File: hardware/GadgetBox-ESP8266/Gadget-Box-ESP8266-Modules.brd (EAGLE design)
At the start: 93.5 x 53.5 mm, 23 parts

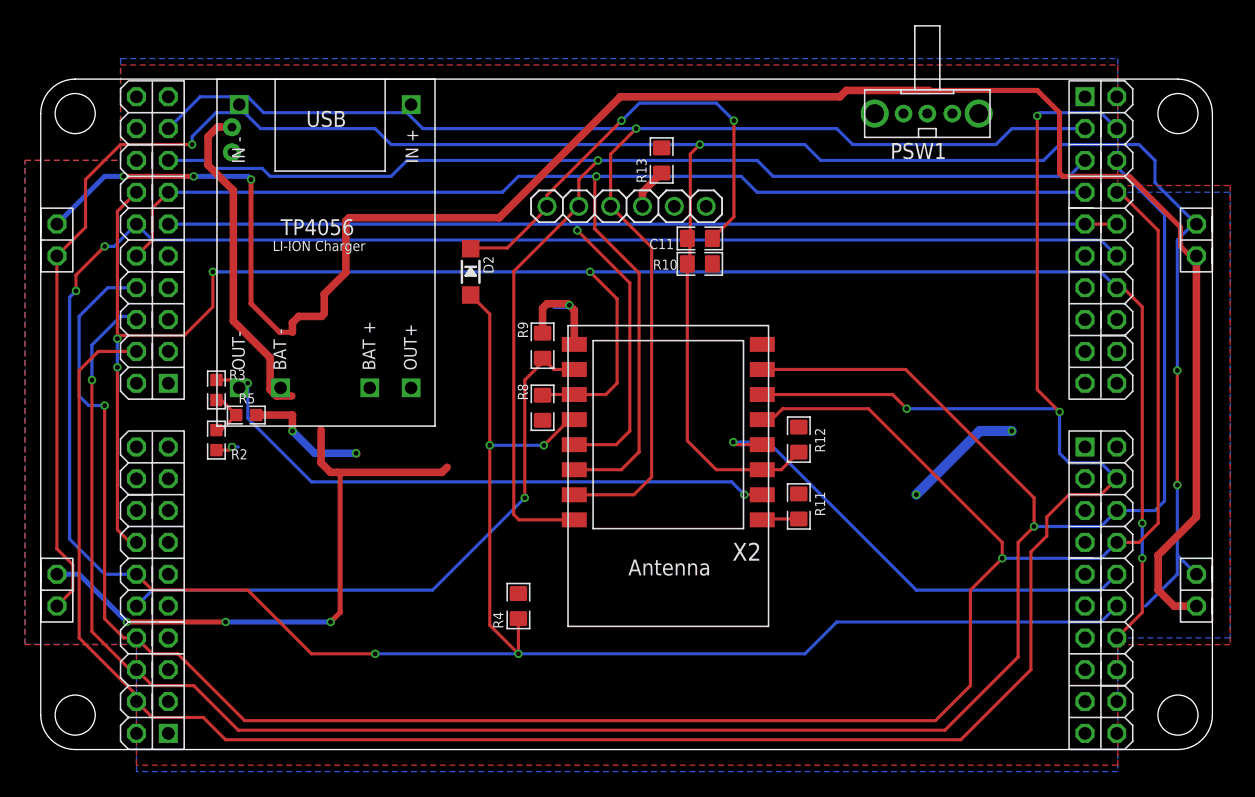
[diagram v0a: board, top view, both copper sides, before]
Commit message: Added battery cutouts and re-routed everything.
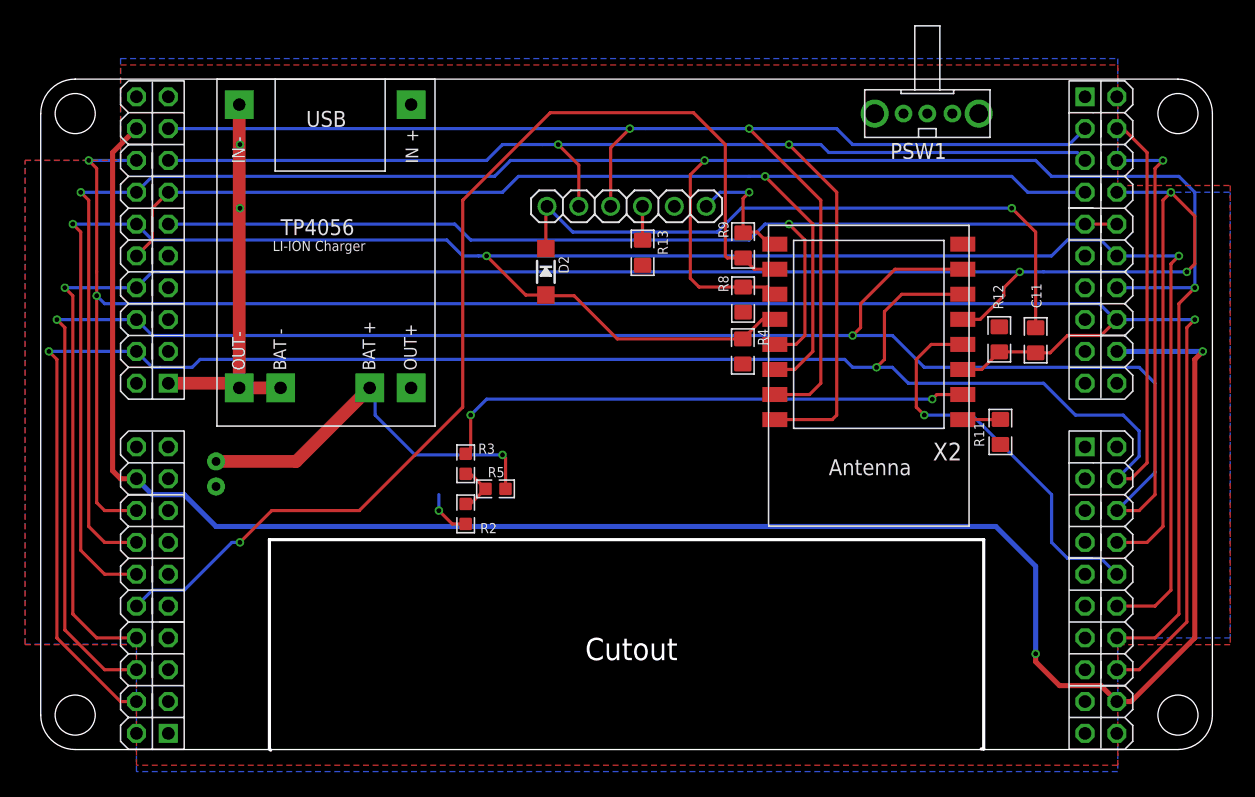
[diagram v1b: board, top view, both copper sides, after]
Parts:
- removed R10: 10K, GadgetFactory:0805
- AH, AL, BH, BL: value ECOGECOG_SLOT_ALT1 -> ECOGECOG_SLOT; device eCogs:ECOG_ALT1 -> eCogs:ECOG
- moved C11 28.0 mm to (80.6, 33.9), turned to 90 degrees
- moved R4 27.1 mm to (57.3, 33.0), turned to 270 degrees
- moved JP1 26.7 mm to (15.2, 23.2)
- moved R2 20.7 mm to (35.2, 20.1)
- moved R3 20.7 mm to (35.2, 24.1)
- moved R5 20.7 mm to (37.5, 22.1)
- moved R8 18.2 mm to (57.3, 37.2)
- moved R12 17.9 mm to (77.7, 34.0)
- moved R9 17.9 mm to (57.3, 41.5)
- moved X2 17.9 mm to (67.3, 32.1)
- moved R11 17.1 mm to (77.8, 26.6), turned to 270 degrees
- moved U$100 13.2 mm to (46.8, 24.0), turned to 0 degrees
- moved R13 7.52 mm to (49.3, 40.9), turned to 270 degrees
- moved D2 6.00 mm to (41.6, 39.4)
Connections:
- net 3V3: no longer R10.2
- net 5V0: now also AH.5V@B7, AL.5V@B7, BH.5V@B7, BL.5V@B7; no longer AH.5V@2, AL.5V@2, BH.5V@2, BL.5V@2
- net RESET: now also AH.RESET@B6, AL.RESET@B6, BH.RESET@B6, BL.RESET@B6; no longer AH.RESET@2, AL.RESET@2, BH.RESET@2, BL.RESET@2, R10.1
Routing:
- net I2C-SDA/BOOTLOAD: track 236.6 -> 180.1 mm, vias 6 -> 3
- net 5V0: track 204.6 -> 158.6 mm, vias 6 -> 2
- net SPI-CSC: track 49.2 -> 87.3 mm
- net GND: track 10.6 -> 45.9 mm, vias 2 -> 4
- net RESET: track 202.2 -> 168.8 mm, vias 4 -> 3
- net I2C-SCL: track 159.7 -> 185.6 mm, vias 6 -> 3
- net SPI-MISO: track 192.4 -> 168.7 mm, vias 3 -> 2
- net DTR: track 37.1 -> 52.5 mm, vias 2 -> 1
- net SPI-SCK: track 182.8 -> 171.6 mm, vias 2 -> 4
- net D2: track 109.6 -> 99.5 mm
- net D3: track 98.8 -> 88.9 mm
- net 3V3: track 9.85 -> 0.00 mm, vias 2 -> 0
- net SPI-MOSI: track 186.2 -> 179.5 mm, vias 2 -> 3
- net SPI-CSD: track 38.4 -> 31.8 mm
- net ADC: track 49.0 -> 43.2 mm
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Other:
- board text added: "- +"
- board text added: "Cutout"
- board text added: "Gadget Box - ESP8266 Copyright 2016 Gadget Factory, LLC Version 1.2-M"
- board text removed: "Gadget Box - ESP8266 Copyright 2016 Gadget Factory, LLC Version 1.1"
